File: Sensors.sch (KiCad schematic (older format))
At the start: 12 parts, among them P4 CONN_01X04, Q1 PMosfetGen, Q2 PMosfetGen, Q4 PMosfetGen, U1 PIR

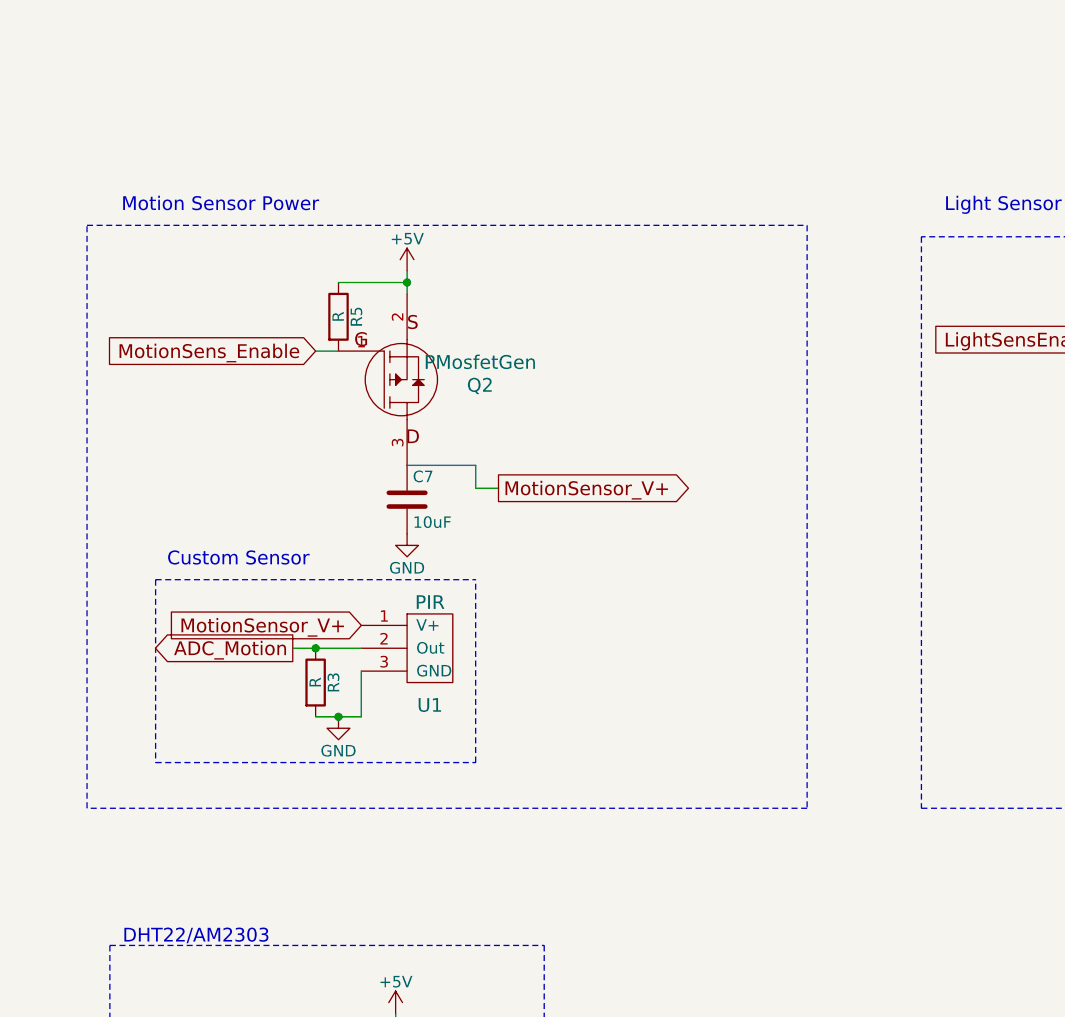
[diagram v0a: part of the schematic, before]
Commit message: Correct some schematics and add todos on pcb
Signed-off-by: Philip Luyckx <philip.luyckx@gmail.com>
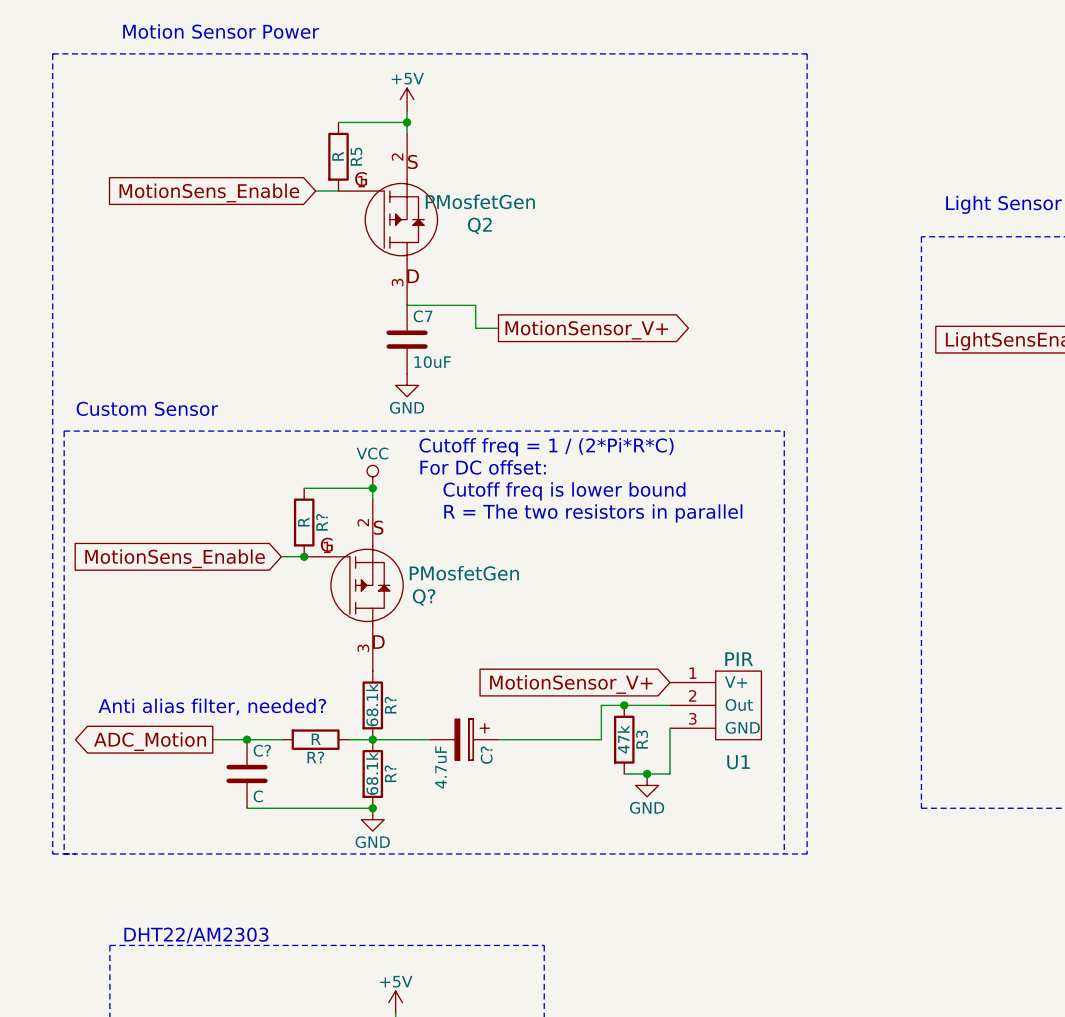
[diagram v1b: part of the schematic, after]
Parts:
- added C?: 4.7uF, symbol CP
- added C?: C, symbol C
- added Q?: PMosfetGen, symbol PMosfetGen
- added R? (x2): 68.1k, symbol R
- added R? (x2): R, symbol R
- R3: value R -> 47k
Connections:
- net ADC_Motion: now also C?.1, R?.2; no longer R3.1, U1.2 (Out)
- net GND: now also C?.2, R?.2
- net MotionSens_Enable: now also Q?.1, R?.2
- net VCC: now also Q?.2, R?.1
- new net: C?.1, R3.1, U1.2 (Out)
- new net: C?.2, R?.1, R?.1, R?.2
- new net: Q?.3, R?.1
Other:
- note added: "Anti alias filter, needed?"
- note added: "Cutoff freq = 1 / (2*Pi*R*C)\nFor DC offset:\n Cutoff freq is lower bound\n R = The two resistors in parallel"
- moved on the sheet: C7, Q2, R3, R5, U1

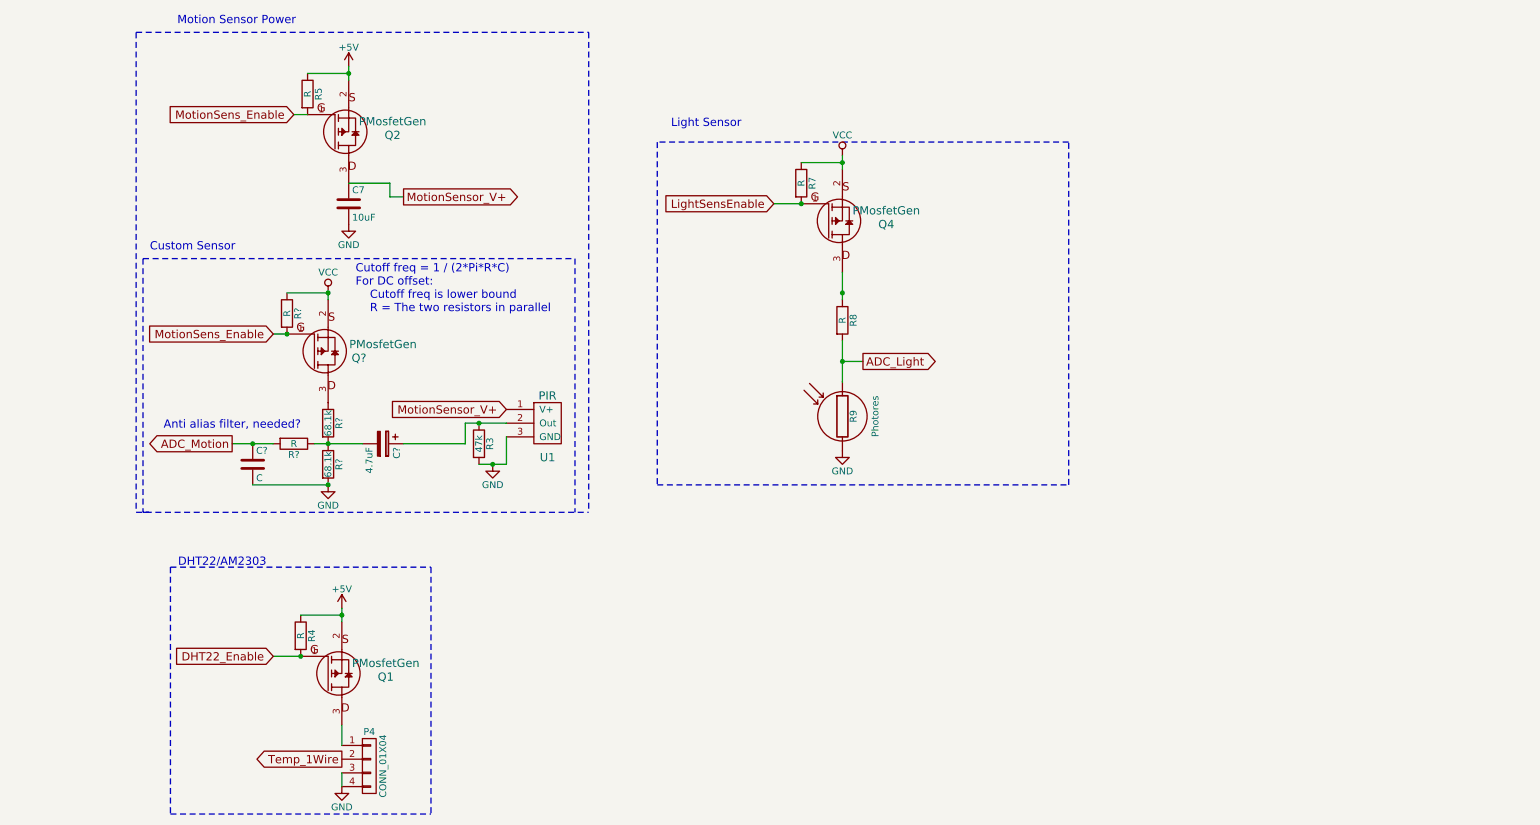
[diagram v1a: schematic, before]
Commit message: Add Opamp circuit
 * Amplify the output of the motion sensor using a AC coupled band
     amplifier.
 * Use one of the opamp circuits as a voltage follower for the light
     sensor to limit the output to 0V and VCC.

Signed-off-by: Philip Luyckx <philip.luyckx@gmail.com>
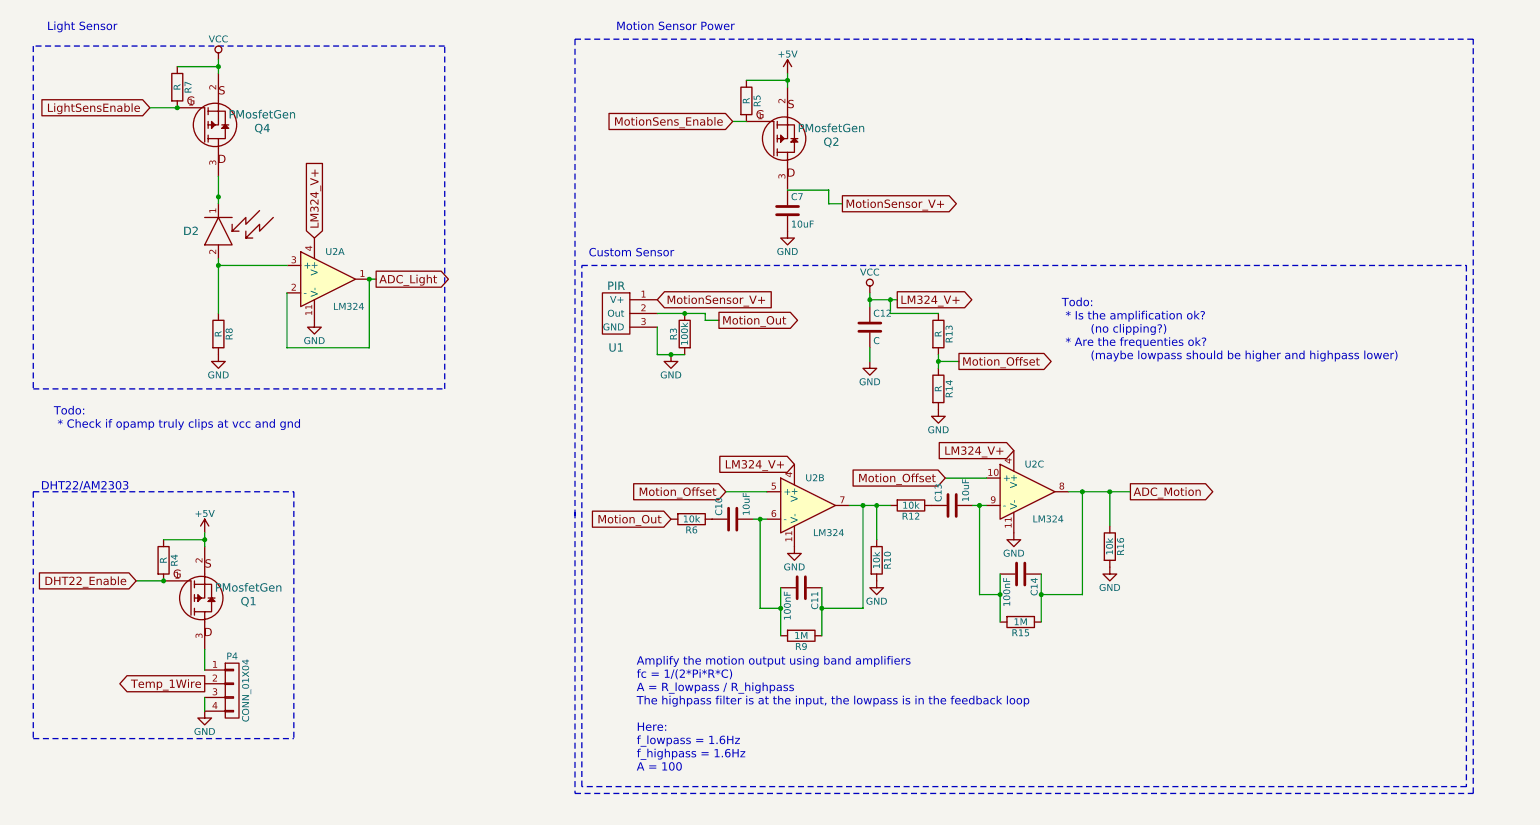
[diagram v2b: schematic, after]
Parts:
- removed C?: 4.7uF, symbol CP
- removed C?: C, symbol C
- removed Q?: PMosfetGen, symbol PMosfetGen
- removed R9: Photores, Resistors_Universal:Resistor_SMD+THTuniversal_1206_RM10_HandSoldering, symbol Photores
- removed R? (x2): 68.1k, symbol R
- removed R? (x2): R, symbol R
- added C10, C13: 10uF, symbol C
- added C11, C14: 100nF, symbol C
- added C12: C, symbol C
- added D2: PhotoDiode, symbol PhotoDiode
- added R10, R12, R16, R6: 10k, symbol R
- added R13, R14: R, symbol R
- added R15, R9: 1M, symbol R
- added U2: LM324, symbol LM324
- R3: value 47k -> 100k
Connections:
- net ADC_Light: now also U2.1, U2.2 (-); no longer R8.2
- net ADC_Motion: now also C14.1, R15.1, R16.1, U2.8
- net GND: now also R8.2, C12.2, R10.2, R14.2, R16.2, U2.11 (V-), U2.11 (V-), U2.11 (V-)
- net VCC: now also C12.1, R13.1, U2.4 (V+), U2.4 (V+), U2.4 (V+)
- net Motion_Out: now reaches R3.1, U1.2 (Out)
- net Motion_Out: now also R6.2
- net at R8.1: now also D2.2, U2.3 (+); no longer Q4.3
- new net: D2.1, Q4.3
- new net: C10.2, C11.2, R9.2, U2.6 (-)
- new net: C11.1, R10.1, R12.2, R9.1, U2.7
- new net: C10.1, R6.1
- new net: C13.2, C14.2, R15.2, U2.9 (-)
- new net: C13.1, R12.1
- new net Motion_Offset: R13.2, R14.1, U2.10 (+), U2.5 (+)
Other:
- note added: "Amplify the motion output using band amplifiers\nfc = 1/(2*Pi*R*C)\nA = R_lowpass / R_highpass\nThe highpass filter is at the input, the lowpass is in the feedback loop\n\nHere:\nf_lowpass = 1.6Hz\nf_highpass = 1.6Hz\nA = 100"
- note added: "Todo:\n * Check if opamp truly clips at vcc and gnd"
- note added: "Todo:\n * Is the amplification ok?\n (no clipping?)\n * Are the frequenties ok?\n (maybe lowpass should be higher and highpass lower)"
- note removed: "Anti alias filter, needed?"
- note removed: "Cutoff freq = 1 / (2*Pi*R*C)\nFor DC offset:\n Cutoff freq is lower bound\n R = The two resistors in parallel"
- moved on the sheet: C7, P4, Q1, Q2, Q4, R3, R4, R5, R7, R8, U1

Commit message: Update schematic and reroute print
 * Update opamp circuit for light sensor
 * Change opamp
 * Reroute everything

Signed-off-by: Philip Luyckx <philip.luyckx@gmail.com>
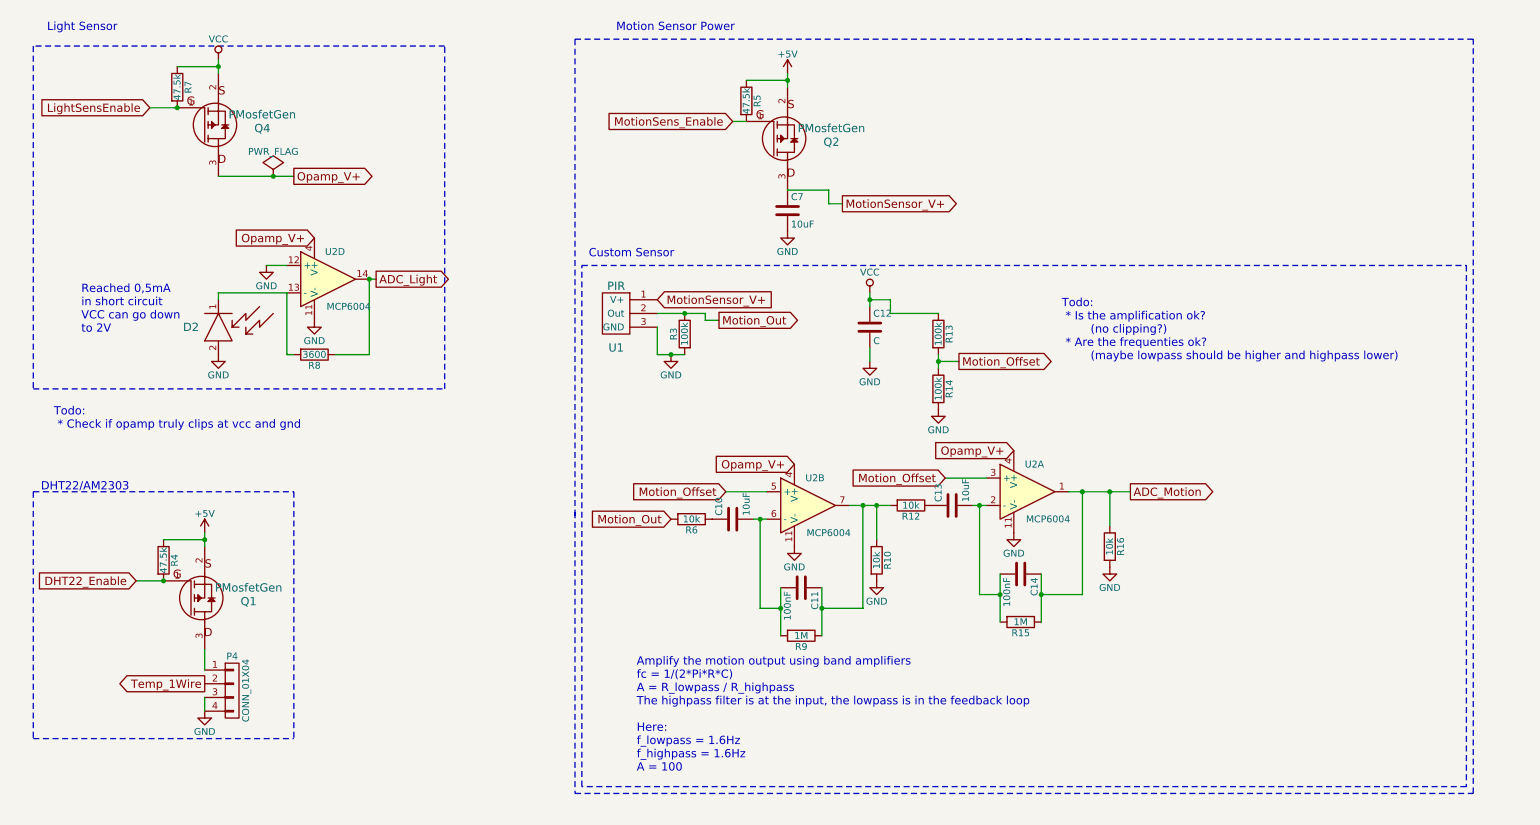
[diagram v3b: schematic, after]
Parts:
- removed U2: LM324, symbol LM324
- added U2: MCP6004, CustomSmd:SOIC-14, symbol MCP6004
- C10, C11, C12, C13, C14: footprint (none) -> Resistors_SMD:R_0805
- D2: footprint (none) -> CustomModules:PD638C
- Q1, Q2, Q4: footprint SMD_Packages:SOT-323 -> CustomSmd:SOT23
- R10, R12, R15, R16, R6, R9: footprint (none) -> Resistors_SMD:R_1206
- R13, R14: value R -> 100k; footprint (none) -> Resistors_SMD:R_1206
- R4, R5, R7: value R -> 47.5k
- R8: value R -> 3600
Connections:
- net ADC_Light: now also R8.1, U2.14
- net ADC_Motion: now also U2.1
- net GND: now also D2.2, U2.11 (V-), U2.11 (V-), U2.11 (V-), U2.12 (+); no longer R8.2
- net Motion_Offset: now also U2.3 (+), U2.5 (+)
- net at D2.1: now also R8.2, U2.13 (-); no longer Q4.3
- net at C10.2, C11.2, R9.2: now also U2.6 (-)
- net at C11.1, R10.1, R12.2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: now also U2.7
- net at C13.2, C14.2, R15.2: now also U2.2 (-)
- new net Opamp_V+: Q4.3, U2.4 (V+), U2.4 (V+), U2.4 (V+)
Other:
- note added: "Reached 0,5mA\nin short circuit\nVCC can go down\nto 2V"
- moved on the sheet: D2, R8

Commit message: Use 0603 resistors
Signed-off-by: Philip Luyckx <philip.luyckx@gmail.com>
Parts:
- R10, R12, R13, R14, R15, R16, R3, R4, R5, R6, R7, R8, R9: footprint Resistors_SMD:R_1206 -> Resistors_SMD:R_0603
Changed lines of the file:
@@
 F 0 "R5" V 5930 1200 50  0000 C CNN
 F 1 "47.5k" V 5850 1200 50  0000 C CNN
-F 2 "Resistors_SMD:R_1206" V 5780 1200 30  0001 C CNN
+F 2 "Resistors_SMD:R_0603" V 5780 1200 30  0001 C CNN
 F 3 "" H 5850 1200 30  0000 C CNN
 	1    5850 1200
@@
 F 0 "R8" V 2780 3050 50  0000 C CNN
 F 1 "3600" V 2700 3050 50  0000 C CNN
-F 2 "Resistors_SMD:R_1206" V 2630 3050 30  0001 C CNN
+F 2 "Resistors_SMD:R_0603" V 2630 3050 30  0001 C CNN
 F 3 "" H 2700 3050 30  0000 C CNN
 	1    2700 3050
@@
 F 0 "R7" V 1780 1100 50  0000 C CNN
 F 1 "47.5k" V 1700 1100 50  0000 C CNN
-F 2 "Resistors_SMD:R_1206" V 1630 1100 30  0001 C CNN
+F 2 "Resistors_SMD:R_0603" V 1630 1100 30  0001 C CNN
 F 3 "" H 1700 1100 30  0000 C CNN
 	1    1700 1100
@@
 F 0 "R4" V 1680 4550 50  0000 C CNN
 F 1 "47.5k" V 1600 4550 50  0000 C CNN
-F 2 "Resistors_SMD:R_1206" V 1530 4550 30  0001 C CNN
+F 2 "Resistors_SMD:R_0603" V 1530 4550 30  0001 C CNN
 F 3 "" H 1600 4550 30  0000 C CNN
 	1    1600 4550
@@
 F 0 "R3" V 5480 2900 50  0000 C CNN
 F 1 "100k" V 5400 2900 50  0000 C CNN
-F 2 "Resistors_SMD:R_1206" V 5330 2900 30  0001 C CNN
+F 2 "Resistors_SMD:R_0603" V 5330 2900 30  0001 C CNN
 F 3 "" H 5400 2900 30  0000 C CNN
 	1    5400 2900
@@
 F 0 "R6" V 5530 4250 50  0000 C CNN
 F 1 "10k" V 5450 4250 50  0000 C CNN
-F 2 "Resistors_SMD:R_1206" V 5380 4250 50  0001 C CNN
+F 2 "Resistors_SMD:R_0603" V 5380 4250 50  0001 C CNN
 F 3 "" H 5450 4250 50  0000 C CNN
 	1    5450 4250
@@
 F 0 "R13" V 7330 2900 50  0000 C CNN
 F 1 "100k" V 7250 2900 50  0000 C CNN
-F 2 "Resistors_SMD:R_1206" V 7180 2900 50  0001 C CNN
+F 2 "Resistors_SMD:R_0603" V 7180 2900 50  0001 C CNN
 F 3 "" H 7250 2900 50  0000 C CNN
 	1    7250 2900
@@
 F 0 "R14" V 7330 3300 50  0000 C CNN
 F 1 "100k" V 7250 3300 50  0000 C CNN
-F 2 "Resistors_SMD:R_1206" V 7180 3300 50  0001 C CNN
+F 2 "Resistors_SMD:R_0603" V 7180 3300 50  0001 C CNN
 F 3 "" H 7250 3300 50  0000 C CNN
 	1    7250 3300
@@
 F 0 "R9" V 6330 5100 50  0000 C CNN
 F 1 "1M" V 6250 5100 50  0000 C CNN
-F 2 "Resistors_SMD:R_1206" V 6180 5100 50  0001 C CNN
+F 2 "Resistors_SMD:R_0603" V 6180 5100 50  0001 C CNN
 F 3 "" H 6250 5100 50  0000 C CNN
 	1    6250 5100
@@
 F 0 "R12" V 7130 4150 50  0000 C CNN
 F 1 "10k" V 7050 4150 50  0000 C CNN
-F 2 "Resistors_SMD:R_1206" V 6980 4150 50  0001 C CNN
+F 2 "Resistors_SMD:R_0603" V 6980 4150 50  0001 C CNN
 F 3 "" H 7050 4150 50  0000 C CNN
 	1    7050 4150
@@
 F 0 "R15" V 7930 5000 50  0000 C CNN
 F 1 "1M" V 7850 5000 50  0000 C CNN
-F 2 "Resistors_SMD:R_1206" V 7780 5000 50  0001 C CNN
+F 2 "Resistors_SMD:R_0603" V 7780 5000 50  0001 C CNN
 F 3 "" H 7850 5000 50  0000 C CNN
 	1    7850 5000
@@
 F 0 "R10" V 6880 4550 50  0000 C CNN
 F 1 "10k" V 6800 4550 50  0000 C CNN
-F 2 "Resistors_SMD:R_1206" V 6730 4550 50  0001 C CNN
+F 2 "Resistors_SMD:R_0603" V 6730 4550 50  0001 C CNN
 F 3 "" H 6800 4550 50  0000 C CNN
 	1    6800 4550
@@
 F 0 "R16" V 8580 4450 50  0000 C CNN
 F 1 "10k" V 8500 4450 50  0000 C CNN
-F 2 "Resistors_SMD:R_1206" V 8430 4450 50  0001 C CNN
+F 2 "Resistors_SMD:R_0603" V 8430 4450 50  0001 C CNN
 F 3 "" H 8500 4450 50  0000 C CNN
 	1    8500 4450

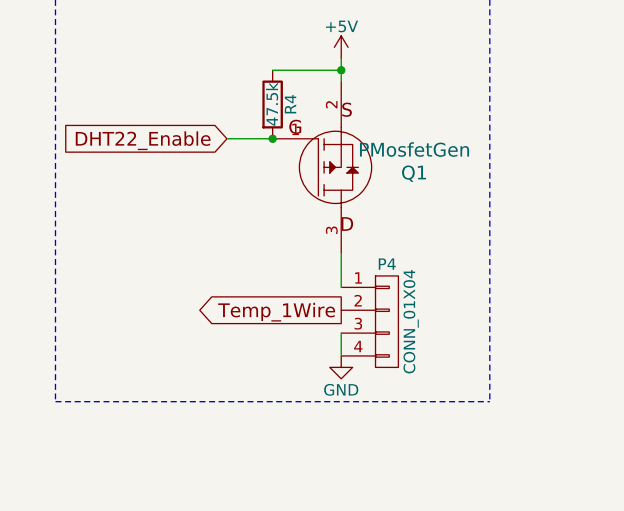
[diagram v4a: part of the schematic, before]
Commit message: Update pull-up resistor for a sensor
Signed-off-by: Philip Luyckx <philip.luyckx@gmail.com>
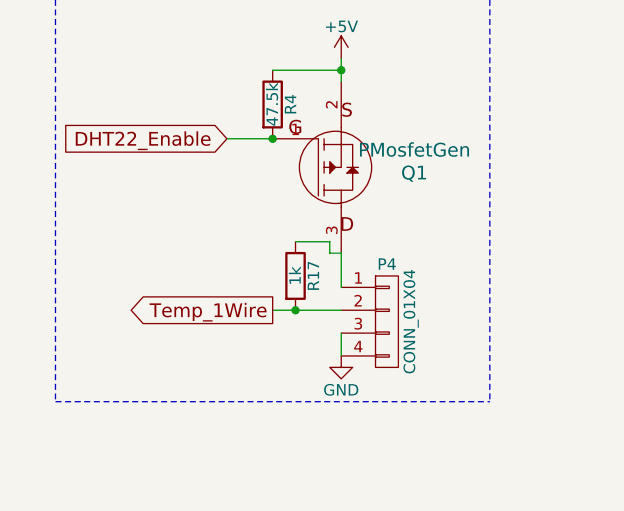
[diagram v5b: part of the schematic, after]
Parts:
- added R17: 1k, Resistors_SMD:R_0603, symbol R
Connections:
- net Temp_1Wire: now also R17.2
- net at P4.1 (P1), Q1.3: now also R17.1
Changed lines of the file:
@@
 	1    0    0    -1
 $EndComp
-Text GLabel 1900 5450 0    60   Output ~ 0
+Text GLabel 1600 5450 0    60   Output ~ 0
 Temp_1Wire
 Text Notes 1350 4050 2    60   ~ 0
@@
 $EndComp
 Connection ~ 2400 1750
+Wire Wire Line
+	1900 5450 1600 5450
+$Comp
+L R R17
+U 1 1 56D88984
+P 1700 5300
+F 0 "R17" V 1780 5300 50  0000 C CNN
+F 1 "1k" V 1700 5300 50  0000 C CNN
+F 2 "Resistors_SMD:R_0603" V 1630 5300 50  0001 C CNN
+F 3 "" H 1700 5300 50  0000 C CNN
+	1    1700 5300
+	1    0    0    -1
+$EndComp
+Connection ~ 1700 5450
+Wire Wire Line
+	1700 5150 1850 5150
+Wire Wire Line
+	1850 5150 1850 5200
+Wire Wire Line
+	1850 5200 1900 5200
 $EndSCHEMATC
